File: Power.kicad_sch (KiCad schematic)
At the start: 17 parts, among them J201 Barrel_Jack, U201 TMA-1215D, U202 LM7805_TO220, U203 LM7905_TO220, U204 LM1117T-3.3

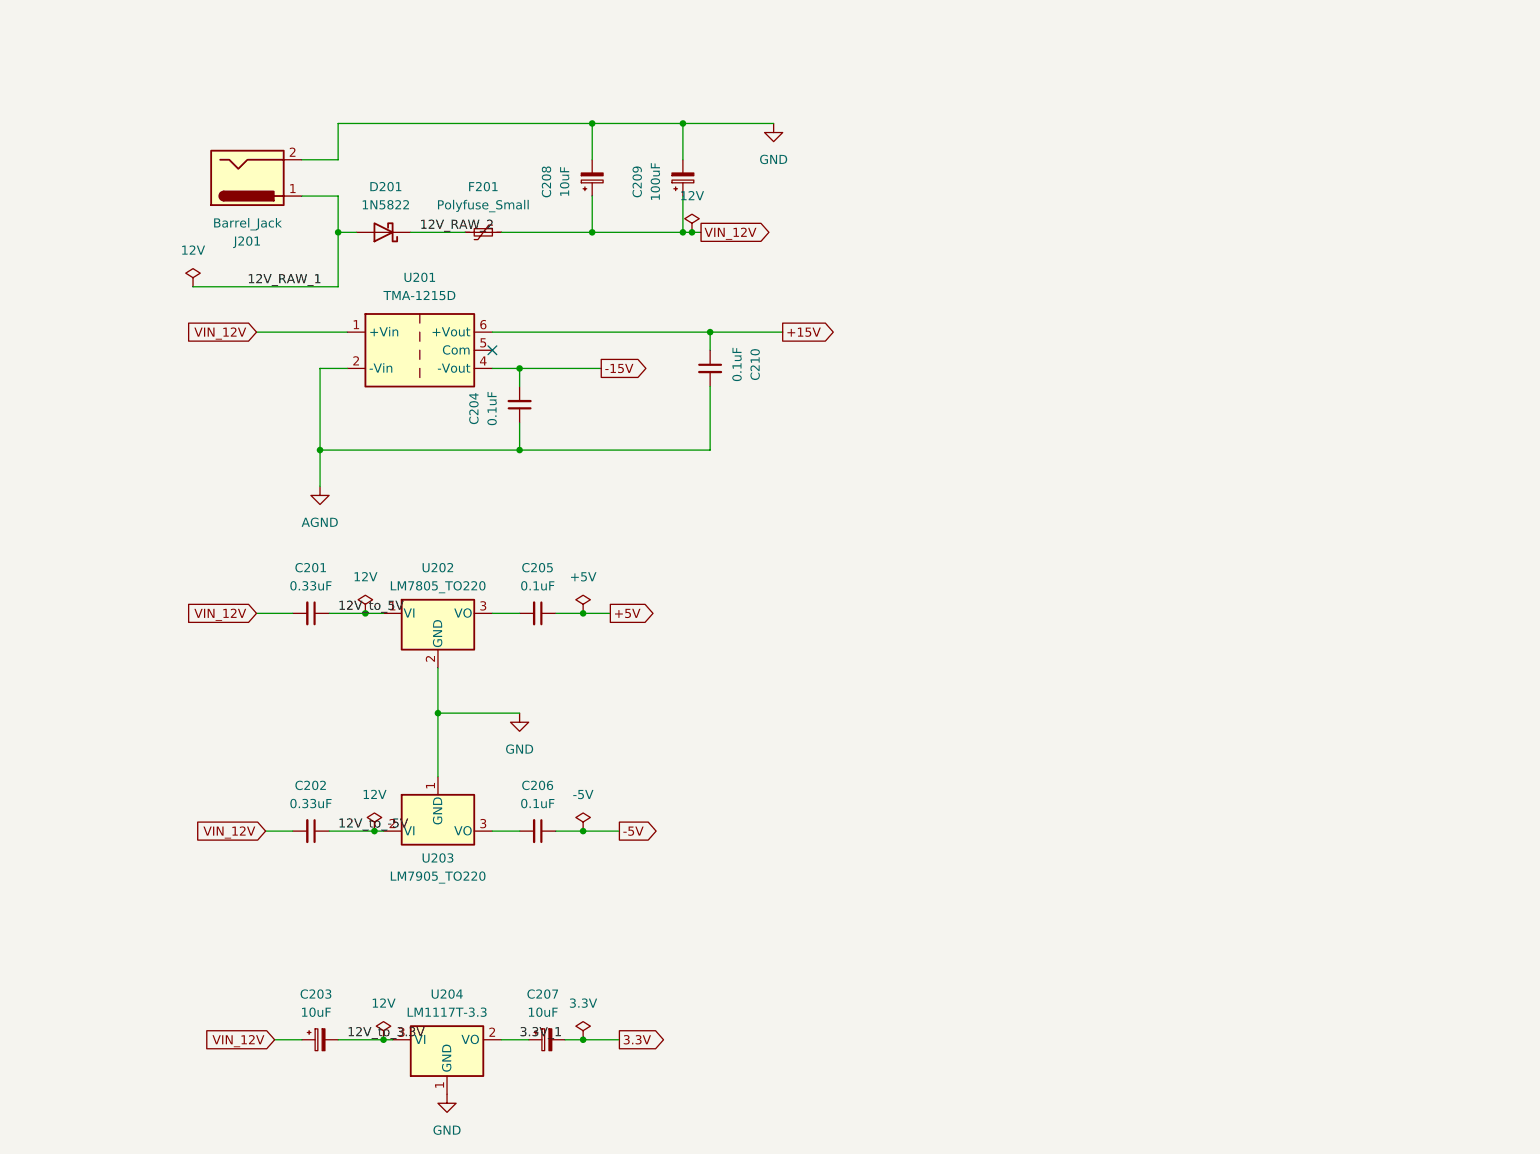
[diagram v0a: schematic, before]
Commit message: New cooler (thermally) power supply.
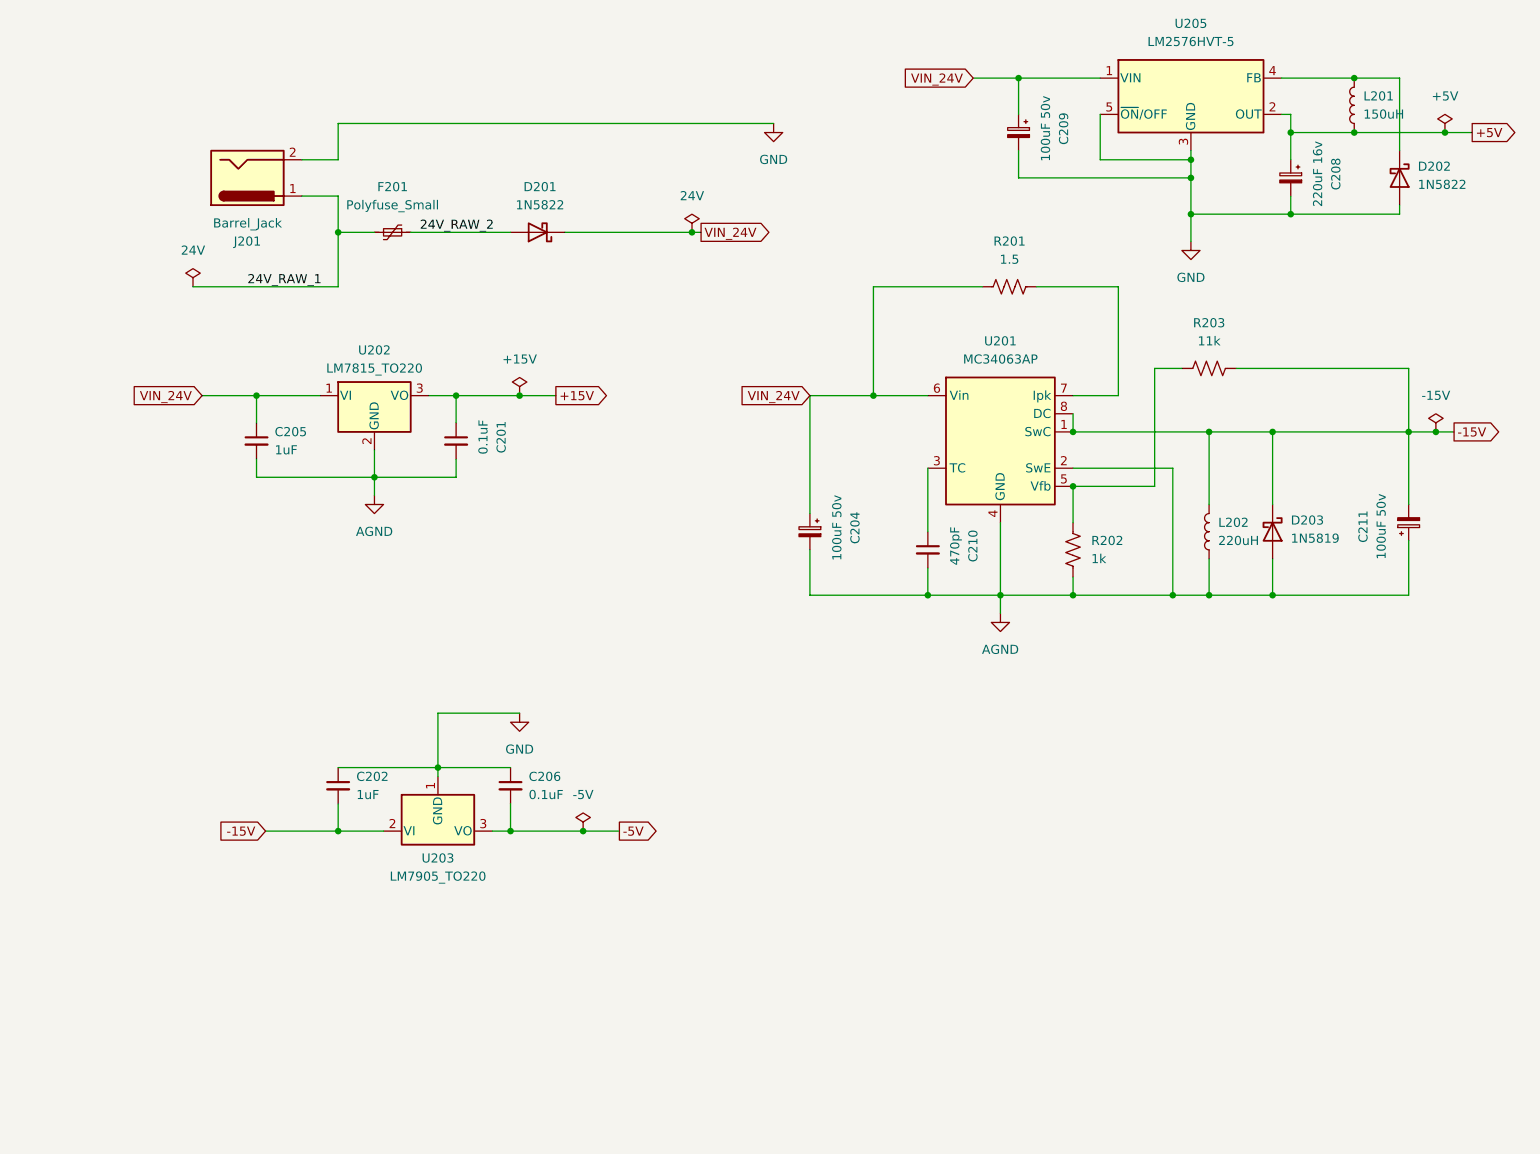
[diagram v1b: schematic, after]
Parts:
- removed C203, C207: 10uF, Capacitor_THT:CP_Radial_D5.0mm_P2.50mm, symbol Device:C_Polarized_Small
- removed C204: 0.1uF, Capacitor_THT:C_Disc_D5.0mm_W2.5mm_P2.50mm, symbol Device:C_Small
- removed U201: TMA-1215D, Converter_DCDC:Converter_DCDC_TRACO_TMA-05xxD_12xxD_Dual_THT, symbol Converter_DCDC:TMA-1215D
- removed U202: LM7805_TO220, Package_TO_SOT_THT:TO-220-3_Vertical, symbol Regulator_Linear:LM7805_TO220
- removed U204: LM1117T-3.3, Package_TO_SOT_THT:TO-220-3_Vertical, symbol Regulator_Linear:LM1117T-3.3
- added C204, C211: 100uF 50v, Capacitor_THT:CP_Radial_D5.0mm_P2.50mm, symbol Device:C_Polarized_Small
- added D202: 1N5822, Diode_THT:D_DO-41_SOD81_P10.16mm_Horizontal, symbol Diode:1N5822
- added D203: 1N5819, Diode_THT:D_DO-41_SOD81_P10.16mm_Horizontal, symbol Diode:1N5819
- added L201: 150uH, Inductor_THT:L_Radial_D10.0mm_P5.00mm_Fastron_07M, symbol Device:L
- added L202: 220uH, Inductor_THT:L_Radial_D10.0mm_P5.00mm_Fastron_07M, symbol Device:L
- added R201: 1.5, Resistor_THT:R_Axial_DIN0207_L6.3mm_D2.5mm_P7.62mm_Horizontal, symbol Device:R_US
- added R202: 1k, Resistor_THT:R_Axial_DIN0207_L6.3mm_D2.5mm_P7.62mm_Horizontal, symbol Device:R_US
- added R203: 11k, Resistor_THT:R_Axial_DIN0207_L6.3mm_D2.5mm_P7.62mm_Horizontal, symbol Device:R_US
- added U201: MC34063AP, Package_DIP:DIP-8_W7.62mm, symbol Regulator_Switching:MC34063AP
- added U202: LM7815_TO220, Package_TO_SOT_THT:TO-220-3_Vertical, symbol Regulator_Linear:LM7815_TO220
- added U205: LM2576HVT-5, Package_TO_SOT_THT:TO-220-5_Vertical, symbol Regulator_Switching:LM2576HVT-5
- C201: value 0.33uF -> 0.1uF
- C202: value 0.33uF -> 1uF
- C205: value 0.1uF -> 1uF
- C208: value 10uF -> 220uF 16v
- C209: value 100uF -> 100uF 50v
- C210: value 0.1uF -> 470pF
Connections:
- net 12V_to_5V is gone; now on net +15V: C201.1
- net +15V: now also U202.3 (VO); no longer C210.1
- net +5V: now also C208.1, L201.1, U205.2 (OUT); no longer C205.1
- net -15V: now also C202.2, U203.2 (VI), C211.2, D203.1 (K), L202.2, R203.2, U201.1 (SwC), U201.8 (DC)
- net -5V: now also C206.2, U203.3 (VO); no longer C206.1
- net AGND: now also C201.2, C205.2, C204.2, C211.1, D203.2 (A), L202.1, R202.2, U201.2 (SwE), U201.4 (GND), U202.2 (GND)
- net GND: now also C202.1, C206.1, D202.2 (A), U205.3 (GND), U205.5 (~{ON}/OFF)
- net 12V_RAW_1 renamed 24V_RAW_1
- net 24V_RAW_1: now also F201.2; no longer D201.2 (A)
- net 12V_RAW_2 renamed VIN_24V
- net VIN_24V: now also C205.1, C209.1, C204.1, R201.1, U201.6 (Vin), U202.1 (VI), U205.1 (VIN); no longer F201.2
- removed net 12V_to_-5V: C202.1, U203.2 (VI)
- removed net VIN_12V: C201.2, C202.2, C208.1, C209.1, F201.1
- new net: C210.1, U201.3 (TC)
- new net: R202.1, R203.1, U201.5 (Vfb)
- new net: R201.2, U201.7 (Ipk)
- new net: D202.1 (K), L201.2, U205.4 (FB)
- new net 24V_RAW_2: D201.2 (A), F201.1
- no-connect marks 1 -> 0
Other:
- moved on the sheet: C202, C205, C206, C208, C209, D201, F201

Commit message: Removed LED Shift registers and replaced them with PCA9685 PWM controllers, Also changed LEDs to RGB LEDs.
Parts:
- renumbered C209 to C201, C208 to C202, C205 to C203, C201 to C204, C211 to C205, C204 to C206, C210 to C207, C202 to C208, C206 to C209, D202 to D201, D201 to D202, R203 to R202, R202 to R203, U205 to U201, U201 to U203, U203 to U204
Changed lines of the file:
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@@
 		(dnp no)
 		(fields_autoplaced yes)
-		(property "Reference" "C202"
+		(property "Reference" "C208"
 			(at 95.25 128.2762 0)
 			(effects
@@
 			(project "circuit"
 				(path "/420e3d7a-6c9a-4806-b4be-05d56aeb21de/52ecec71-1c0e-4647-a50f-721f168ee7e0"
-					(reference "C202")
+					(reference "C208")
 					(unit 1)
 				)
@@
 		(on_board yes)
 		(dnp no)
-		(property "Reference" "C208"
+		(property "Reference" "C202"
 			(at 232.41 43.9039 90)
 			(effects
@@
 			(project "circuit"
 				(path "/420e3d7a-6c9a-4806-b4be-05d56aeb21de/52ecec71-1c0e-4647-a50f-721f168ee7e0"
-					(reference "C208")
+					(reference "C202")
 					(unit 1)
 				)
@@
 		(dnp no)
 		(fields_autoplaced yes)
-		(property "Reference" "#PWR0206"
+		(property "Reference" "#PWR0203"
 			(at 97.79 95.25 0)
 			(effects
@@
 			(project "circuit"
 				(path "/420e3d7a-6c9a-4806-b4be-05d56aeb21de/52ecec71-1c0e-4647-a50f-721f168ee7e0"
-					(reference "#PWR0206")
+					(reference "#PWR0203")
 					(unit 1)
 				)
@@
 		(on_board yes)
 		(dnp no)
-		(property "Reference" "C210"
+		(property "Reference" "C207"
 			(at 181.61 95.9739 90)
 			(effects
@@
 			(project "circuit"
 				(path "/420e3d7a-6c9a-4806-b4be-05d56aeb21de/52ecec71-1c0e-4647-a50f-721f168ee7e0"
-					(reference "C210")
+					(reference "C207")
 					(unit 1)
 				)
@@
 		(dnp no)
 		(fields_autoplaced yes)
-		(property "Reference" "#PWR0201"
+		(property "Reference" "#PWR0204"
 			(at 185.42 111.76 0)
 			(effects
@@
 			(project "circuit"
 				(path "/420e3d7a-6c9a-4806-b4be-05d56aeb21de/52ecec71-1c0e-4647-a50f-721f168ee7e0"
-					(reference "#PWR0201")
+					(reference "#PWR0204")
 					(unit 1)
 				)
@@
 		(dnp no)
 		(fields_autoplaced yes)
-		(property "Reference" "#PWR0204"
+		(property "Reference" "#PWR0201"
 			(at 153.67 43.18 0)
 			(effects
@@
 			(project "circuit"
 				(path "/420e3d7a-6c9a-4806-b4be-05d56aeb21de/52ecec71-1c0e-4647-a50f-721f168ee7e0"
-					(reference "#PWR0204")
+					(reference "#PWR0201")
 					(unit 1)
 				)
@@
 		(on_board yes)
 		(dnp no)
-		(property "Reference" "C201"
+		(property "Reference" "C204"
 			(at 115.57 80.7339 90)
 			(effects
@@
 			(project "circuit"
 				(path "/420e3d7a-6c9a-4806-b4be-05d56aeb21de/52ecec71-1c0e-4647-a50f-721f168ee7e0"
-					(reference "C201")
+					(reference "C204")
 					(unit 1)
 				)
@@
 		(dnp no)
 		(fields_autoplaced yes)
-		(property "Reference" "#PWR0203"
+		(property "Reference" "#PWR0205"
 			(at 118.11 125.73 0)
 			(effects
@@
 			(project "circuit"
 				(path "/420e3d7a-6c9a-4806-b4be-05d56aeb21de/52ecec71-1c0e-4647-a50f-721f168ee7e0"
-					(reference "#PWR0203")
+					(reference "#PWR0205")
 					(unit 1)
 				)
@@
 		(on_board yes)
 		(dnp no)
-		(property "Reference" "R203"
+		(property "Reference" "R202"
 			(at 214.63 64.77 90)
 			(effects
@@
 			(project "circuit"
 				(path "/420e3d7a-6c9a-4806-b4be-05d56aeb21de/52ecec71-1c0e-4647-a50f-721f168ee7e0"
-					(reference "R203")
+					(reference "R202")
 					(unit 1)
 				)
@@
 		(on_board yes)
 		(dnp no)
-		(property "Reference" "C204"
+		(property "Reference" "C206"
 			(at 165.1 93.4339 90)
 			(effects
@@
 			(project "circuit"
 				(path "/420e3d7a-6c9a-4806-b4be-05d56aeb21de/52ecec71-1c0e-4647-a50f-721f168ee7e0"
-					(reference "C204")
+					(reference "C206")
 					(unit 1)
 				)
@@
 		(dnp no)
 		(fields_autoplaced yes)
-		(property "Reference" "U205"
+		(property "Reference" "U201"
 			(at 212.09 22.86 0)
 			(effects
@@
 			(project ""
 				(path "/420e3d7a-6c9a-4806-b4be-05d56aeb21de/52ecec71-1c0e-4647-a50f-721f168ee7e0"
-					(reference "U205")
+					(reference "U201")
 					(unit 1)
 				)
@@
 		(dnp no)
 		(fields_autoplaced yes)
-		(property "Reference" "#FLG0205"
+		(property "Reference" "#FLG0201"
 			(at 247.65 36.195 0)
 			(effects
@@
 			(project "circuit"
 				(path "/420e3d7a-6c9a-4806-b4be-05d56aeb21de/52ecec71-1c0e-4647-a50f-721f168ee7e0"
-					(reference "#FLG0205")
+					(reference "#FLG0201")
 					(unit 1)
 				)
@@
 		(dnp no)
 		(fields_autoplaced yes)
-		(property "Reference" "#FLG0209"
+		(property "Reference" "#FLG0205"
 			(at 246.38 78.105 0)
 			(effects
@@
 			(project "circuit"
 				(path "/420e3d7a-6c9a-4806-b4be-05d56aeb21de/52ecec71-1c0e-4647-a50f-721f168ee7e0"
-					(reference "#FLG0209")
+					(reference "#FLG0205")
 					(unit 1)
 				)
@@
 		(dnp no)
 		(fields_autoplaced yes)
-		(property "Reference" "#FLG0201"
+		(property "Reference" "#FLG0203"
 			(at 72.39 57.785 0)
 			(effects
@@
 			(project "circuit"
 				(path "/420e3d7a-6c9a-4806-b4be-05d56aeb21de/52ecec71-1c0e-4647-a50f-721f168ee7e0"
-					(reference "#FLG0201")
+					(reference "#FLG0203")
 					(unit 1)
 				)
@@
 		(dnp no)
 		(fields_autoplaced yes)
-		(property "Reference" "C205"
+		(property "Reference" "C203"
 			(at 83.82 80.0162 0)
 			(effects
@@
 			(project "circuit"
 				(path "/420e3d7a-6c9a-4806-b4be-05d56aeb21de/52ecec71-1c0e-4647-a50f-721f168ee7e0"
-					(reference "C205")
+					(reference "C203")
 					(unit 1)
 				)
@@
 		(dnp no)
 		(fields_autoplaced yes)
-		(property "Reference" "#FLG0208"
+		(property "Reference" "#FLG0202"
 			(at 142.24 50.165 0)
 			(effects
@@
 			(project "circuit"
 				(path "/420e3d7a-6c9a-4806-b4be-05d56aeb21de/52ecec71-1c0e-4647-a50f-721f168ee7e0"
-					(reference "#FLG0208")
+					(reference "#FLG0202")
 					(unit 1)
 				)
@@
 		(on_board yes)
 		(dnp no)
-		(property "Reference" "C211"
+		(property "Reference" "C205"
 			(at 236.22 93.2561 90)
 			(effects
@@
 			(project "circuit"
 				(path "/420e3d7a-6c9a-4806-b4be-05d56aeb21de/52ecec71-1c0e-4647-a50f-721f168ee7e0"
-					(reference "C211")
+					(reference "C205")
 					(unit 1)
 				)
@@
 		(dnp no)
 		(fields_autoplaced yes)
-		(property "Reference" "C206"
+		(property "Reference" "C209"
 			(at 119.38 128.2762 0)
 			(effects
@@
 			(project "circuit"
 				(path "/420e3d7a-6c9a-4806-b4be-05d56aeb21de/52ecec71-1c0e-4647-a50f-721f168ee7e0"
-					(reference "C206")
+					(reference "C209")
 					(unit 1)
 				)
@@
 		(dnp no)
 		(fields_autoplaced yes)
-		(property "Reference" "#FLG0202"
+		(property "Reference" "#FLG0204"
 			(at 118.11 73.025 0)
 			(effects
@@
 			(project "circuit"
 				(path "/420e3d7a-6c9a-4806-b4be-05d56aeb21de/52ecec71-1c0e-4647-a50f-721f168ee7e0"
-					(reference "#FLG0202")
+					(reference "#FLG0204")
 					(unit 1)
 				)
@@
 		(dnp no)
 		(fields_autoplaced yes)
-		(property "Reference" "U203"
+		(property "Reference" "U204"
 			(at 106.68 139.7 0)
 			(effects
@@
 			(project "circuit"
 				(path "/420e3d7a-6c9a-4806-b4be-05d56aeb21de/52ecec71-1c0e-4647-a50f-721f168ee7e0"
-					(reference "U203")
+					(reference "U204")
 					(unit 1)
 				)
@@
 		(dnp no)
 		(fields_autoplaced yes)
-		(property "Reference" "D202"
+		(property "Reference" "D201"
 			(at 243.84 42.8624 90)
 			(effects
@@
 			(project "circuit"
 				(path "/420e3d7a-6c9a-4806-b4be-05d56aeb21de/52ecec71-1c0e-4647-a50f-721f168ee7e0"
-					(reference "D202")
+					(reference "D201")
 					(unit 1)
 				)
@@
 		(dnp no)
 		(fields_autoplaced yes)
-		(property "Reference" "#PWR0205"
+		(property "Reference" "#PWR0202"
 			(at 212.09 59.69 0)
 			(effects
@@
 			(project "circuit"
 				(path "/420e3d7a-6c9a-4806-b4be-05d56aeb21de/52ecec71-1c0e-4647-a50f-721f168ee7e0"
-					(reference "#PWR0205")
+					(reference "#PWR0202")
 					(unit 1)
 				)
@@
 		(dnp no)
 		(fields_autoplaced yes)
-		(property "Reference" "U201"
+		(property "Reference" "U203"
 			(at 185.42 67.31 0)
 			(effects
@@
 			(project ""
 				(path "/420e3d7a-6c9a-4806-b4be-05d56aeb21de/52ecec71-1c0e-4647-a50f-721f168ee7e0"
-					(reference "U201")
+					(reference "U203")
 					(unit 1)
 				)
@@
 		(dnp no)
 		(fields_autoplaced yes)
-		(property "Reference" "D201"
+		(property "Reference" "D202"
 			(at 120.9675 45.72 0)
 			(effects
@@
 			(project "circuit"
 				(path "/420e3d7a-6c9a-4806-b4be-05d56aeb21de/52ecec71-1c0e-4647-a50f-721f168ee7e0"
-					(reference "D201")
+					(reference "D202")
 					(unit 1)
 				)
@@
 		(dnp no)
 		(fields_autoplaced yes)
-		(property "Reference" "R202"
+		(property "Reference" "R203"
 			(at 198.12 95.2499 0)
 			(effects
@@
 			(project "circuit"
 				(path "/420e3d7a-6c9a-4806-b4be-05d56aeb21de/52ecec71-1c0e-4647-a50f-721f168ee7e0"
-					(reference "R202")
+					(reference "R203")
 					(unit 1)
 				)
@@
 		(on_board yes)
 		(dnp no)
-		(property "Reference" "C209"
+		(property "Reference" "C201"
 			(at 194.31 37.5539 90)
 			(effects
@@
 			(project "circuit"
 				(path "/420e3d7a-6c9a-4806-b4be-05d56aeb21de/52ecec71-1c0e-4647-a50f-721f168ee7e0"
-					(reference "C209")
-					(unit 1)
-				)
+					(reference "C201")
+					(unit 1)
+				)
